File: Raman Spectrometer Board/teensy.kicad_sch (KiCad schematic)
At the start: 1 part, among them U2 Teensy4.1_DEV-16771

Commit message: Added footprints to main board
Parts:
- U2: footprint MODULE_DEV-16771 -> MRDT_Shields:Teensy_4_1_Ethernet
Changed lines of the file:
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@@
 			)
 		)
-		(property "Footprint" "MODULE_DEV-16771"
+		(property "Footprint" "MRDT_Shields:Teensy_4_1_Ethernet"
 			(at 204.47 109.22 0)
 			(effects

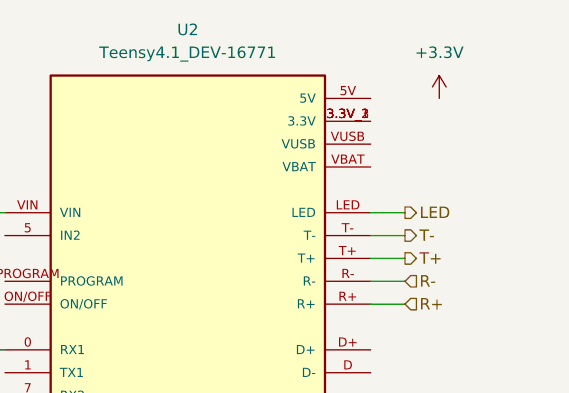
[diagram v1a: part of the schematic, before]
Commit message: loose voltage connected
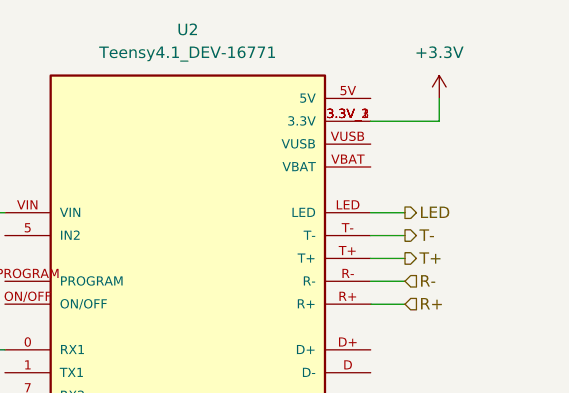
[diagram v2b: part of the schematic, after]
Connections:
- net +3.3V: now also U2.3.3V_1 (3.3V), U2.3.3V_2 (3.3V), U2.3.3V_3 (3.3V)
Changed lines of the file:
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@@
+	(wire
+		(pts
+			(xy 171.45 55.88) (xy 179.07 55.88)
+		)
+		(stroke
+			(width 0)
+			(type default)
+		)
+	)
 	(wire
 		(pts
@@
 		)
 		(stroke
+			(width 0)
+			(type default)
+		)
+	)
+	(wire
+		(pts
+			(xy 179.07 53.34) (xy 179.07 55.88)
+		)
+		(stroke

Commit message: tof voltages connected
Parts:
- U2: footprint MRDT_Shields:Teensy_4_1_Ethernet -> MODULE_DEV-16771
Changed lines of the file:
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@@
 			)
 		)
-		(property "Footprint" "MRDT_Shields:Teensy_4_1_Ethernet"
+		(property "Footprint" "MODULE_DEV-16771"
 			(at 204.47 109.22 0)
 			(effects

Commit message: Revert "tof voltages connected"
This reverts commit cb392bf1d60e7f863b02c943ae62205c2a2451bd.
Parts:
- U2: footprint MODULE_DEV-16771 -> MRDT_Shields:Teensy_4_1_Ethernet
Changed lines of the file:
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@@
 			)
 		)
-		(property "Footprint" "MODULE_DEV-16771"
+		(property "Footprint" "MRDT_Shields:Teensy_4_1_Ethernet"
 			(at 204.47 109.22 0)
 			(effects

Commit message: Page Consolidation
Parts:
- added C1: .1uF, Capacitor_SMD:C_0603_1608Metric_Pad1.08x0.95mm_HandSolder, symbol Device:C
- added J3: RJ45_LED_Shielded, MRDT_Connectors:RJ45_Teensy, symbol Connector:RJ45_LED_Shielded
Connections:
- net GND: now also C1.2, J3.8, J3.9, J3.SH
- net LED: now also J3.10
- net R+: now also J3.4
- net R-: now also J3.6
- net T+: now also J3.1
- net T-: now also J3.3
- new net: C1.1, J3.2, J3.5
- no-connect marks 0 -> 3
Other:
- moved on the sheet: U2

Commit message: Fixed CAN page
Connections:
- no-connect marks 3 -> 34
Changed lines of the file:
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@@
+	)
+	(no_connect
+		(at 85.09 86.36)
+	)
+	(no_connect
+		(at 125.73 111.76)
+	)
+	(no_connect
+		(at 125.73 81.28)
+	)
+	(no_connect
+		(at 125.73 121.92)
+	)
+	(no_connect
+		(at 85.09 76.2)
+	)
+	(no_connect
+		(at 85.09 88.9)
+	)
+	(no_connect
+		(at 125.73 134.62)
+	)
+	(no_connect
+		(at 85.09 91.44)
+	)
+	(no_connect
+		(at 85.09 111.76)
+	)
+	(no_connect
+		(at 85.09 68.58)
+	)
+	(no_connect
+		(at 85.09 93.98)
+	)
+	(no_connect
+		(at 85.09 127)
 	)
 	(no_connect
@@
 	)
 	(no_connect
+		(at 125.73 142.24)
+	)
+	(no_connect
+		(at 85.09 83.82)
+	)
+	(no_connect
+		(at 125.73 83.82)
+	)
+	(no_connect
+		(at 125.73 106.68)
+	)
+	(no_connect
+		(at 85.09 121.92)
+	)
+	(no_connect
+		(at 125.73 132.08)
+	)
+	(no_connect
+		(at 85.09 124.46)
+	)
+	(no_connect
 		(at 198.12 62.23)
+	)
+	(no_connect
+		(at 125.73 127)
+	)
+	(no_connect
+		(at 85.09 109.22)
+	)
+	(no_connect
+		(at 125.73 124.46)
+	)
+	(no_connect
+		(at 85.09 73.66)
+	)
+	(no_connect
+		(at 85.09 104.14)
+	)
+	(no_connect
+		(at 85.09 96.52)
 	)
 	(no_connect
 		(at 177.8 77.47)
 	)
+	(no_connect
+		(at 85.09 142.24)
+	)
+	(no_connect
+		(at 125.73 96.52)
+	)
+	(no_connect
+		(at 85.09 101.6)
+	)
+	(no_connect
+		(at 85.09 139.7)
+	)
+	(no_connect
+		(at 125.73 129.54)
+	)
+	(no_connect
+		(at 85.09 99.06)
+	)
 	(wire

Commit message: TOF and CCD Connector Layout
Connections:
- net +3.3V renamed +3V3
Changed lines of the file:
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@@
+	)
+	(symbol
+		(lib_id "power:+3V3")
+		(at 133.35 53.34 0)
+		(unit 1)
+		(exclude_from_sim no)
+		(in_bom yes)
+		(on_board yes)
+		(dnp no)
+		(fields_autoplaced yes)
+		(property "Reference" "#PWR023"
+			(at 133.35 57.15 0)
+			(effects
+				(font
+					(size 1.27 1.27)
+				)
+				(hide yes)
+			)
+		)
+		(property "Value" "+3V3"
+			(at 133.35 48.26 0)
+			(effects
+				(font
+					(size 1.27 1.27)
+				)
+			)
+		)
+		(property "Footprint" ""
+			(at 133.35 53.34 0)
+			(effects
+				(font
+					(size 1.27 1.27)
+				)
+				(hide yes)
+			)
+		)
+		(property "Datasheet" ""
+			(at 133.35 53.34 0)
+			(effects
+				(font
+					(size 1.27 1.27)
+				)
+				(hide yes)
+			)
+		)
+		(property "Description" "Power symbol creates a global label with name \"+3V3\""
+			(at 133.35 53.34 0)
+			(effects
+				(font
+					(size 1.27 1.27)
+				)
+				(hide yes)
+			)
+		)
+		(pin "1"
+		)
+		(instances
+			(project ""
+				(path "/ab487c59-f066-48f5-a383-99e8eaf806bf/d2cb0292-9da9-4449-86d5-dc8d83eb4083"
+					(reference "#PWR023")
+					(unit 1)
+				)
+			)
+		)
 	)
 	(symbol
@@
 					(unit 1)
 				)
-			)
-		)
-	)
-	(symbol
-		(lib_id "power:+3.3V")
-		(at 133.35 53.34 0)
-		(unit 1)
-		(exclude_from_sim no)
-		(in_bom yes)
-		(on_board yes)
-		(dnp no)
-		(fields_autoplaced yes)
-		(property "Reference" "#PWR023"
-			(at 133.35 57.15 0)
-			(effects
-				(font
-					(size 1.27 1.27)
-				)
-				(hide yes)
-			)
-		)
-		(property "Value" "+3.3V"
-			(at 133.35 48.26 0)
-			(effects
-				(font
-					(size 1.27 1.27)
-				)
-			)
-		)
-		(property "Footprint" ""
-			(at 133.35 53.34 0)
-			(effects
-				(font
-					(size 1.27 1.27)
-				)
-				(hide yes)
-			)
-		)
-		(property "Datasheet" ""
-			(at 133.35 53.34 0)
-			(effects
-				(font
-					(size 1.27 1.27)
-				)
-				(hide yes)
-			)
-		)
-		(property "Description" "Power symbol creates a global label with name \"+3.3V\""
-			(at 133.35 53.34 0)
-			(effects
-				(font
-					(size 1.27 1.27)
-				)
-				(hide yes)
-			)
-		)
-		(pin "1"
-		)
-		(instances
-			(project ""
-				(path "/ab487c59-f066-48f5-a383-99e8eaf806bf/d2cb0292-9da9-4449-86d5-dc8d83eb4083"
-					(reference "#PWR023")
-					(unit 1)
-				)

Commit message: CAN Layout
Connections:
- net CRX: now also U2.23 (A9); no longer U2.11 (MOSI)
- net CTX: now also U2.22 (A8); no longer U2.13 (SCK)
- net CTX2: now reaches U2.30 (CRX3)
- net CRX2: now reaches U2.31 (CTX3)
- net STDBY2: now reaches U2.32 (OUT1B)
- no-connect marks 34 -> 29
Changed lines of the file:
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@@
-	)
-	(no_connect
-		(at 125.73 142.24)
 	)
 	(no_connect
@@
 	)
 	(no_connect
-		(at 85.09 104.14)
-	)
-	(no_connect
 		(at 85.09 96.52)
 	)
@@
 	)
 	(no_connect
-		(at 85.09 142.24)
-	)
-	(no_connect
-		(at 125.73 96.52)
-	)
-	(no_connect
-		(at 85.09 101.6)
-	)
-	(no_connect
 		(at 85.09 139.7)
 	)
@@
 	(wire
 		(pts
+			(xy 125.73 142.24) (xy 129.54 142.24)
+		)
+		(stroke
+			(width 0)
+			(type default)
+		)
+	)
+	(wire
+		(pts
 			(xy 177.8 59.69) (xy 165.1 59.69)
 		)
@@
 	(wire
 		(pts
+			(xy 80.01 142.24) (xy 85.09 142.24)
+		)
+		(stroke
+			(width 0)
+			(type default)
+		)
+	)
+	(wire
+		(pts
 			(xy 198.12 67.31) (xy 207.01 67.31)
 		)
@@
 	(wire
 		(pts
+			(xy 80.01 101.6) (xy 85.09 101.6)
+		)
+		(stroke
+			(width 0)
+			(type default)
+		)
+	)
+	(wire
+		(pts
 			(xy 80.01 81.28) (xy 85.09 81.28)
 		)
@@
 		(pts
 			(xy 125.73 71.12) (xy 129.54 71.12)
+		)
+		(stroke
+			(width 0)
+			(type default)
+		)
+	)
+	(wire
+		(pts
+			(xy 80.01 104.14) (xy 85.09 104.14)
+		)
+		(stroke
+			(width 0)
+			(type default)
+		)
+	)
+	(wire
+		(pts
+			(xy 125.73 96.52) (xy 129.54 96.52)
 		)
 		(stroke
@@
 		)
 	)
+	(hierarchical_label "STDBY2"
+		(shape output)
+		(at 129.54 96.52 0)
+		(effects
+			(font
+				(size 1.27 1.27)
+			)
+			(justify left)
+		)
+	)
+	(hierarchical_label "CRX"
+		(shape input)
+		(at 129.54 142.24 0)
+		(effects
+			(font
+				(size 1.27 1.27)
+			)
+			(justify left)
+		)
+	)
+	(hierarchical_label "CTX2"
+		(shape output)
+		(at 80.01 101.6 180)
+		(effects
+			(font
+				(size 1.27 1.27)
+			)
+			(justify right)
+		)
+	)
 	(hierarchical_label "GPIP"
 		(shape output)
@@
 			)
 			(justify left)
+		)
+	)
+	(hierarchical_label "CRX2"
+		(shape input)
+		(at 80.01 104.14 180)
+		(effects
+			(font
+				(size 1.27 1.27)
+			)
+			(justify right)
 		)
 	)
@@
 		)
 	)
+	(hierarchical_label "CTX"
+		(shape output)
+		(at 80.01 142.24 180)
+		(effects
+			(font
+				(size 1.27 1.27)
+			)
+			(justify right)
+		)
+	)
 	(hierarchical_label "fanOut"
 		(shape output)
@@
 		)
 	)
-	(hierarchical_label "CRX"
-		(shape input)
-		(at 129.54 114.3 0)
+	(hierarchical_label "diodeOutput"
+		(shape output)
+		(at 80.01 114.3 180)
+		(effects
+			(font
+				(size 1.27 1.27)
+			)
+			(justify right)
+		)
+	)
+	(hierarchical_label "Servo2"
+		(shape output)
+		(at 129.54 104.14 0)
 		(effects
 			(font
@@
 		)
 	)
-	(hierarchical_label "diodeOutput"
-		(shape output)
-		(at 80.01 114.3 180)
-		(effects
-			(font
-				(size 1.27 1.27)
-			)
-			(justify right)
-		)
-	)
-	(hierarchical_label "Servo2"
-		(shape output)
-		(at 129.54 104.14 0)
-		(effects
-			(font
-				(size 1.27 1.27)
-			)
-			(justify left)
-		)
-	)
-	(hierarchical_label "CTX"
-		(shape output)
-		(at 80.01 116.84 180)
-		(effects
-			(font
-				(size 1.27 1.27)
-			)
-			(justify right)
-		)
-	)
